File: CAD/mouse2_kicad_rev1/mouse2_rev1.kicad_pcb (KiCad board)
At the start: 2 copper layers, 101 parts, among them IC1 STM32F405RGT6, J2 SWD Header, M1 M1_Conn_Alt, M2 M2_Conn_Alt, Q0 TEFT4300, Q1 TEFT4300, Q10 Q_NMOS_GSD, Q11 Q_NMOS_GSD, Q12 Q_NMOS_GSD, Q2 TEFT4300, Q3 TEFT4300, Q9 Q_NMOS_GSD, SW1 SW, SW2 SW, SW3 SW, U10 TPS7A2033PDBVR, U2 L293D, U3 TLV70019_SOT23-5, U4 BC832, U5 LM66100DCKR, U6 LM66100DCKR, U7 ICM-45605, U8 TPS7A2033PDBVR, U9 TS30011-M050QFNR

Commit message: Mouse 2 is ballin ish! got a bunch of layout done
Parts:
- removed C38: 22uF, Capacitor_SMD:C_0805_2012Metric_Pad1.18x1.45mm_HandSolder
- removed C40: 0.1uF, Capacitor_SMD:C_0805_2012Metric_Pad1.18x1.45mm_HandSolder
- removed MOS1: SSM3K335R_LF, custom_foot:SOT-23F_TOS
- removed RST1, SW1, SW2, SW3: SW, Button_Switch_SMD:SW_SPST_REED_CT05-XXXX-G1
- removed U6: LM66100DCKR, custom_foot:DCK6_TEX
- added C10: 0.1uF, Capacitor_SMD:C_0603_1608Metric_Pad1.08x0.95mm_HandSolder, F.Cu at (210.6, 126.2)
- added C11: 0.1uF, Capacitor_SMD:C_0603_1608Metric_Pad1.08x0.95mm_HandSolder, F.Cu at (200.5, 111.1)
- added C12: 0.1uF, Capacitor_SMD:C_0603_1608Metric_Pad1.08x0.95mm_HandSolder, F.Cu at (188.0, 132.9)
- added C13: 4.7uF, Capacitor_SMD:C_0603_1608Metric_Pad1.08x0.95mm_HandSolder, F.Cu at (207.8, 110.6)
- added C16: 10uF, Capacitor_SMD:C_0603_1608Metric_Pad1.08x0.95mm_HandSolder, F.Cu at (202.5, 110.6)
- added C17: 0.1uF, Capacitor_SMD:C_0603_1608Metric_Pad1.08x0.95mm_HandSolder, F.Cu at (202.7, 108.3)
- added C18: 47uF, Capacitor_SMD:C_0603_1608Metric_Pad1.08x0.95mm_HandSolder, F.Cu at (233.2, 143.4)
- added C22: 15pF, Capacitor_SMD:C_0603_1608Metric_Pad1.08x0.95mm_HandSolder, F.Cu at (230.6, 141.6)
- added C23: 22uF, Capacitor_SMD:C_0603_1608Metric_Pad1.08x0.95mm_HandSolder, F.Cu at (165.0, 136.5)
- added C24: 15pF, Capacitor_SMD:C_0603_1608Metric_Pad1.08x0.95mm_HandSolder, F.Cu at (230.6, 139.0)
- added C25: 0.1uF, Capacitor_SMD:C_0603_1608Metric_Pad1.08x0.95mm_HandSolder, F.Cu at (166.0, 142.1)
- added C26: 10uF, Capacitor_SMD:C_0603_1608Metric_Pad1.08x0.95mm_HandSolder, F.Cu at (166.0, 144.1)
- added D10: LED, LED_SMD:LED_0805_2012Metric_Pad1.15x1.40mm_HandSolder, F.Cu at (120.7, 105.6)
- added D8: 1SS389,L3F, Diode_SMD:D_SOD-523, F.Cu at (120.1, 116.0)
- added D9: 1SS389,L3F, Diode_SMD:D_SOD-523, F.Cu at (120.1, 118.4)
- added J1: SWD Header, Connector_PinHeader_2.54mm:PinHeader_1x05_P2.54mm_Vertical, F.Cu at (125.4, 94.2)
- added R10: 10k, Resistor_SMD:R_0603_1608Metric_Pad0.98x0.95mm_HandSolder, F.Cu at (200.5, 126.8)
- added R22: 13, Resistor_SMD:R_0603_1608Metric_Pad0.98x0.95mm_HandSolder, F.Cu at (206.9, 126.2)
- added R23: 47K, Resistor_SMD:R_0603_1608Metric_Pad0.98x0.95mm_HandSolder, F.Cu at (117.6, 68.1)
- added R25: 47K, Resistor_SMD:R_0603_1608Metric_Pad0.98x0.95mm_HandSolder, F.Cu at (117.6, 73.1)
- added R28: 47K, Resistor_SMD:R_0603_1608Metric_Pad0.98x0.95mm_HandSolder, F.Cu at (117.6, 80.6)
- added S1: SKRPABE010, BUTTON:SW_SKRPABE010, F.Cu at (110.0, 94.3)
- added S3: SKRPABE010, BUTTON:SW_SKRPABE010, F.Cu at (110.0, 99.0)
- added S4: SKRPABE010, BUTTON:SW_SKRPABE010, F.Cu at (110.0, 103.8)
- added S6: SKRPABE010, BUTTON:SW_SKRPABE010, F.Cu at (110.0, 108.5)
- added U1: PMW3389DM-T3QU, PMW3389:PMW3360DM, F.Cu at (208.6, 113.5)
- added U11: LM66100DCKR, custom_foot:DCK6_TEX, F.Cu at (120.7, 112.8)
- added Y1: ABS07-32.768KHZ-T, AS07-XTAL:XTAL_ABS07-32.768KHZ-T, F.Cu at (233.7, 140.3)
- added Y2: 16MHz, Crystal:Crystal_SMD_2016-4Pin_2.0x1.6mm, F.Cu at (211.2, 135.5)
- C14, C15, C20, C27, C28, C29, C3, C30, C31, C32, C33, C34, C39, C8, C9: footprint Capacitor_SMD:C_1206_3216Metric_Pad1.33x1.80mm_HandSolder -> Capacitor_SMD:C_0603_1608Metric_Pad1.08x0.95mm_HandSolder
- C19: value 0.1uF -> 10uF; footprint Capacitor_SMD:C_1206_3216Metric_Pad1.33x1.80mm_HandSolder -> Capacitor_SMD:C_0603_1608Metric_Pad1.08x0.95mm_HandSolder
- C21: value 1uF -> 0.1uF; footprint Capacitor_SMD:C_1206_3216Metric_Pad1.33x1.80mm_HandSolder -> Capacitor_SMD:C_0603_1608Metric_Pad1.08x0.95mm_HandSolder
- C35, C36: value 10uF -> 0.1uF; footprint Capacitor_SMD:C_1206_3216Metric_Pad1.33x1.80mm_HandSolder -> Capacitor_SMD:C_0603_1608Metric_Pad1.08x0.95mm_HandSolder
- C37: footprint Capacitor_SMD:C_0805_2012Metric_Pad1.18x1.45mm_HandSolder -> Capacitor_SMD:C_0603_1608Metric_Pad1.08x0.95mm_HandSolder
- C4: value 0.1uF -> 1uF; footprint Capacitor_SMD:C_1206_3216Metric_Pad1.33x1.80mm_HandSolder -> Capacitor_SMD:C_0603_1608Metric_Pad1.08x0.95mm_HandSolder
- C7: value 10uF -> 0.1uF
- R1, R11, R19, R2, R20, R21, R24, R26, R3, R4, R5, R6, R7, R8, R9: footprint Resistor_SMD:R_1206_3216Metric_Pad1.30x1.75mm_HandSolder -> Resistor_SMD:R_0603_1608Metric_Pad0.98x0.95mm_HandSolder
- R12: value 47K -> 75; footprint Resistor_SMD:R_1206_3216Metric_Pad1.30x1.75mm_HandSolder -> Resistor_SMD:R_0603_1608Metric_Pad0.98x0.95mm_HandSolder
- R13, R14, R15: value 47k -> 47K; footprint Resistor_SMD:R_1206_3216Metric_Pad1.30x1.75mm_HandSolder -> Resistor_SMD:R_0603_1608Metric_Pad0.98x0.95mm_HandSolder
- R16: value 47k -> 10k; footprint Resistor_SMD:R_1206_3216Metric_Pad1.30x1.75mm_HandSolder -> Resistor_SMD:R_0603_1608Metric_Pad0.98x0.95mm_HandSolder
- R17, R27: value 10K -> 10k; footprint Resistor_SMD:R_1206_3216Metric_Pad1.30x1.75mm_HandSolder -> Resistor_SMD:R_0603_1608Metric_Pad0.98x0.95mm_HandSolder
- R18: value 20K -> 20k; footprint Resistor_SMD:R_1206_3216Metric_Pad1.30x1.75mm_HandSolder -> Resistor_SMD:R_0603_1608Metric_Pad0.98x0.95mm_HandSolder
- moved M1 186.9 mm to (288.8, 121.7), turned to 90 degrees
- moved M2 170.6 mm to (272.1, 121.7), turned to -90 degrees
- moved C3 160.2 mm to (295.0, 96.0)
- moved C35 152.2 mm to (303.7, 113.5)
- moved U2 148.1 mm to (276.6, 118.1)
- moved Q11 141.4 mm to (239.5, 79.9), turned to 180 degrees
- moved R3 127.7 mm to (244.8, 77.9), turned to 90 degrees
- moved R7 126.0 mm to (240.9, 76.9), turned to 180 degrees
- moved R15 120.8 mm to (242.8, 79.9), turned to 90 degrees
- moved U4 120.0 mm to (240.1, 142.3), turned to 180 degrees
- moved Q12 116.9 mm to (204.2, 71.9), turned to 180 degrees
- moved D2 114.3 mm to (241.5, 74.9), turned to 180 degrees
- moved C20 106.2 mm to (247.0, 77.9), turned to -90 degrees
- moved Q10 101.6 mm to (193.2, 73.8), turned to 180 degrees
- moved Q2 97.5 mm to (247.0, 74.9), turned to 180 degrees
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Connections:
- C1 pad 2: AGND -> GND
- C14 pad 1: +3V3A -> VDDA
- C14 pad 2: AGND -> GND
- C15 pad 1: +3V3A -> VDDA
- C15 pad 2: AGND -> GND
- C19 pad 1: RST -> VDDA
- C2 pad 1: +1V9 -> MOUSE_VDD
- C2 pad 2: AGND -> GND
- C20 pad 1: +3V3A -> VDDA
- C20 pad 2: AGND -> GND
- C21 pad 1: +3V3A -> GND
- C21 pad 2: AGND -> VDD
- C27 pad 1: VDD -> GND
- C27 pad 2: GND -> VDD
- C28 pad 1: VDD -> GND
- C28 pad 2: GND -> VDD
- C29 pad 1: VDD -> GND
- C29 pad 2: GND -> VDD
- C31 pad 1: VDDA -> GND
- C31 pad 2: GND -> VDDA
- C32 pad 1: VDD -> GND
- C32 pad 2: GND -> VDD
- C34 pad 1: VCAP_2 -> VCAP_1
- C35 pad 1: VDDA -> GND
- C35 pad 2: GND -> +5V
- C36 pad 1: BATT_NET -> Net-(D8-K)
- C36 pad 2: PGND -> GND
- C37 pad 1: +5V_NET -> +5V
- C4 pad 1: +5V -> VDDA
- C44 pad 1: +3V3A -> VDDA
- C44 pad 2: AGND -> GND
- C5 pad 1: unconnected-(C5-Pad1) -> MOUSE_VDD
- C5 pad 2: unconnected-(C5-Pad2) -> GND
- C6 pad 1: unconnected-(C6-Pad1) -> VDD
- C6 pad 2: unconnected-(C6-Pad2) -> GND
- C7 pad 1: unconnected-(C7-Pad1) -> VDD
- C7 pad 2: unconnected-(C7-Pad2) -> GND
- C8 pad 1: VDD -> GND
- C8 pad 2: GND -> VDD
- C9 pad 1: unconnected-(C9-Pad1) -> VDDPIX
- C9 pad 2: unconnected-(C9-Pad2) -> GND
- D7 pad 1: POWER_LED -> GND
- IC1 pad 12: VSSA -> GND
- IC1 pad 18: VSS -> GND
- IC1 pad 40: POWER_LED -> unconnected-(IC1-PC9-Pad40)
- IC1 pad 5: unconnected-(IC1-PH0-Pad5) -> Net-(IC1-PH0)
- IC1 pad 50: unconnected-(IC1-PA15-Pad50) -> MOUSE_CS
- IC1 pad 51: unconnected-(IC1-PC10-Pad51) -> BC_RX_STM_TX
- IC1 pad 52: unconnected-(IC1-PC11-Pad52) -> BC_TX_STM_RX
- IC1 pad 53: unconnected-(IC1-PC12-Pad53) -> MOUSE_PICO
- IC1 pad 55: unconnected-(IC1-PB3-Pad55) -> MOUSE_SCLK
- IC1 pad 56: unconnected-(IC1-PB4-Pad56) -> MOUSE_POCI
- IC1 pad 63: VSS -> GND
- L2 pad 2: +5V_NET -> +5V
- NT2 pad 2: AGND -> PGND
- Q0 pad 1: +3V3A -> VDDA
- Q1 pad 1: +3V3A -> VDDA
- Q2 pad 1: +3V3A -> VDDA
- Q3 pad 1: +3V3A -> VDDA
- R1 pad 1: AGND -> GND
- R12 pad 1: VDD -> Net-(D10-A)
- R12 pad 2: RST -> VDD
- R13 pad 1: GND -> EMIT_2
- R13 pad 2: EMIT_1 -> GND
- R14 pad 1: GND -> EMIT_3
- R14 pad 2: EMIT_2 -> GND
- R15 pad 1: GND -> EMIT_4
- R15 pad 2: EMIT_4 -> GND
- R16 pad 1: GND -> VDD
- R16 pad 2: EMIT_3 -> IMU_POCI
- R17 pad 1: GND -> BOOT0
- R17 pad 2: BOOT0 -> GND
- R2 pad 1: AGND -> GND
- R24 pad 1: VDD -> EMIT_1
- R24 pad 2: BUTTON_2 -> GND
- R3 pad 1: AGND -> GND
- R4 pad 1: AGND -> GND
- S2 pad 2: BATT_NET -> VCC
- U10 pad 2: AGND -> GND
- U10 pad 5: +3V3A -> VDDA
- U3 pad 2: AGND -> GND
- U3 pad 5: +1V9 -> MOUSE_VDD
- U4 pad 1: unconnected-(U4-GND-Pad1) -> GND
- U4 pad 10: unconnected-(U4-P21/RESET-Pad10) -> BC_RST
- U4 pad 11: unconnected-(U4-P00/XL1-Pad11) -> Net-(U4-P00/XL1)
- U4 pad 12: unconnected-(U4-P01/XL2-Pad12) -> Net-(U4-P01/XL2)
- U4 pad 16: unconnected-(U4-VDD-Pad16) -> VDD
- U4 pad 2: unconnected-(U4-P20/LED-Pad2) -> BC_LED
- U4 pad 3: unconnected-(U4-SWDIO-Pad3) -> BC_SWDIO
- U4 pad 4: unconnected-(U4-SWCLK-Pad4) -> BC_SWDCLK
- U4 pad 7: unconnected-(U4-P11/RX-Pad7) -> BC_RX_STM_TX
- U4 pad 8: unconnected-(U4-P12/TX-Pad8) -> BC_TX_STM_RX
- U5 pad 3: +5V_NET -> +5V
- U7 pad 5: +3V3A -> VDD
- U7 pad 6: AGND -> GND
- U7 pad 8: +3V3A -> VDDA
- U9 pad 11: BATT_NET -> VCC
- U9 pad 2: BATT_NET -> VCC
- U9 pad 3: BATT_NET -> VCC
- U9 pad 5: +5V_NET -> +5V
- U9 pad 9: BATT_NET -> unconnected-(U9-EN-Pad9)
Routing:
- net VDD: track 0.00 -> 63.8 mm
- net MOUSE_VDD: track 0.00 -> 50.3 mm
- net VCC: track 0.00 -> 36.8 mm, vias 0 -> 2
- net PGND: track 0.00 -> 29.3 mm, vias 0 -> 4
- net +5V: track 0.00 -> 22.6 mm
- net VDDA: track 0.00 -> 18.1 mm
- net Net-(C39-Pad2): track 0.00 -> 14.5 mm
- net IMU_CS: track 0.00 -> 14.2 mm, vias 0 -> 2
- net IMU_SCLK: track 0.00 -> 11.5 mm, vias 0 -> 2
- net IMU_PICO: track 0.00 -> 9.44 mm
- net IMU_POCI: track 0.00 -> 8.66 mm
- net Net-(U4-P00/XL1): track 0.00 -> 5.51 mm
- net GND: track 0.00 -> 4.92 mm, vias 0 -> 4
- net Net-(U4-P01/XL2): track 0.00 -> 4.89 mm
- net RECEIV_3: track 0.00 -> 4.80 mm
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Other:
- board outline added: 92.8 x 94.6 mm

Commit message: rev2 done !
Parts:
- removed C36: 0.1uF, Capacitor_SMD:C_0603_1608Metric_Pad1.08x0.95mm_HandSolder
- removed R10, R16: 10k, Resistor_SMD:R_0603_1608Metric_Pad0.98x0.95mm_HandSolder
- removed SK1, SK2, SK3, SK4: M2, MountingHole:MountingHole_2.2mm_M2
- removed TP7: V_EXT_TP, Connector_PinHeader_2.54mm:PinHeader_1x01_P2.54mm_Vertical
- added C38: 0.1uF, Capacitor_SMD:C_0603_1608Metric_Pad1.08x0.95mm_HandSolder, F.Cu at (232.0, 134.2)
- added C40: 0.1uF, Capacitor_SMD:C_0603_1608Metric_Pad1.08x0.95mm_HandSolder, F.Cu at (232.0, 130.2)
- moved R12 147.0 mm to (247.1, 133.8)
- moved R21 142.1 mm to (247.0, 121.8)
- moved R26 140.3 mm to (247.0, 129.8)
- moved C3 139.3 mm to (157.8, 119.4), turned to 90 degrees
- moved R9 139.1 mm to (237.3, 128.3), turned to 90 degrees
- moved R20 138.3 mm to (247.0, 125.8)
- moved R19 137.0 mm to (247.0, 117.8)
- moved S3 136.1 mm to (241.8, 128.3)
- moved RST1 134.3 mm to (241.8, 134.1)
- moved S2 133.9 mm to (241.8, 122.6)
- moved S1 132.4 mm to (241.8, 116.8)
- moved R11 132.4 mm to (237.3, 116.8), turned to 90 degrees
- moved R23 132.2 mm to (234.2, 130.2), turned to -90 degrees
- moved R25 131.7 mm to (234.2, 134.2), turned to -90 degrees
- moved D5 130.1 mm to (247.0, 127.8), turned to 180 degrees
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- renumbered M_MH2 to M_MH1, M_MH1 to M_MH2, S2 to PWR1, S6 to RST1, S4 to S1, S3 to S2, S1 to S3
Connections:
- M1 pad 1: M2_OUT_1 -> GND
- M1 pad 2: M2_OUT_2 -> M1_ENC_B
- M1 pad 3: VDD -> M1_ENC_A
- M1 pad 4: M2_ENC_A -> VDD
- M1 pad 5: M2_ENC_B -> M1_OUT_2
- M1 pad 6: GND -> M1_OUT_1
- M2 pad 1: M1_OUT_1 -> GND
- M2 pad 2: M1_OUT_2 -> M2_ENC_B
- M2 pad 3: VDD -> M2_ENC_A
- M2 pad 4: M1_ENC_A -> VDD
- M2 pad 5: M1_ENC_B -> M2_OUT_2
- M2 pad 6: GND -> M2_OUT_1
- PWR1 pad 3: Net-(S2-Pad3) -> unconnected-(PWR1-Pad3)
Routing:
- net +5V: track 22.6 -> 301.3 mm, vias 0 -> 1
- net VDD: track 63.8 -> 283.0 mm, vias 0 -> 11
- net VDDA: track 18.1 -> 198.9 mm
- net EMIT_4: track 2.33 -> 97.2 mm, vias 0 -> 2
- net RECEIV_4: track 2.21 -> 94.4 mm, vias 0 -> 1
- net EMIT_1: track 2.33 -> 82.7 mm, vias 0 -> 2
- net RECEIV_3: track 4.80 -> 85.1 mm, vias 0 -> 1
- net LED_RED: track 0.00 -> 79.6 mm, vias 0 -> 2
- net RECEIV_1: track 2.21 -> 79.5 mm, vias 0 -> 1
- net RECEIV_2: track 2.47 -> 79.0 mm, vias 0 -> 1
- net EMIT_3: track 2.33 -> 77.3 mm, vias 0 -> 2
- net LED_BLUE: track 0.00 -> 73.1 mm, vias 0 -> 2
- net EMIT_2: track 2.33 -> 71.5 mm, vias 0 -> 2
- net M1_ENC_A: track 0.00 -> 68.1 mm, vias 0 -> 2
- net M1_ENC_B: track 0.00 -> 67.0 mm, vias 0 -> 2
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- added copper zone on B.Cu, net GND
- added copper zone on F.Cu, net GND
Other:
- board text added: "AirLiteTalonFX"
- board text added: "Rev. 2.0 | By Rezq"

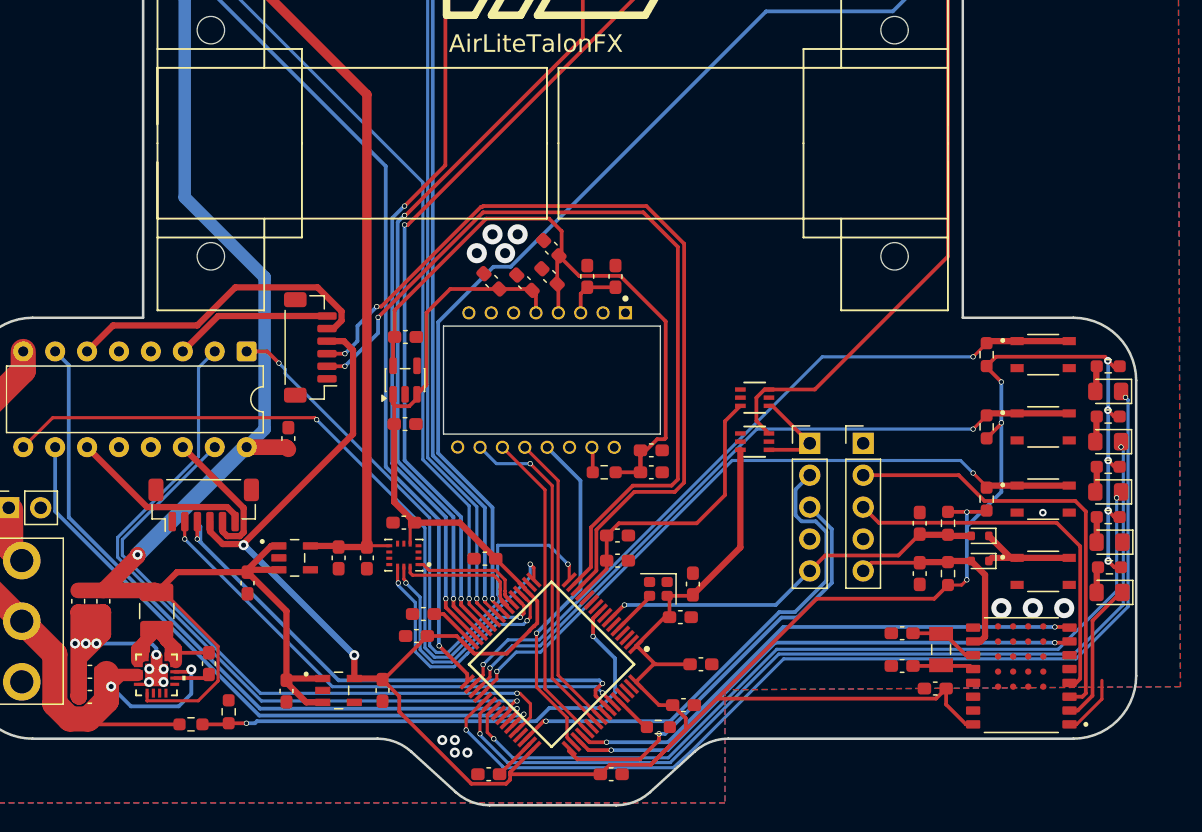
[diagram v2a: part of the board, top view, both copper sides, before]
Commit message: Micromouse is assembled and turns on! LEDs work as well. IOC is updated.
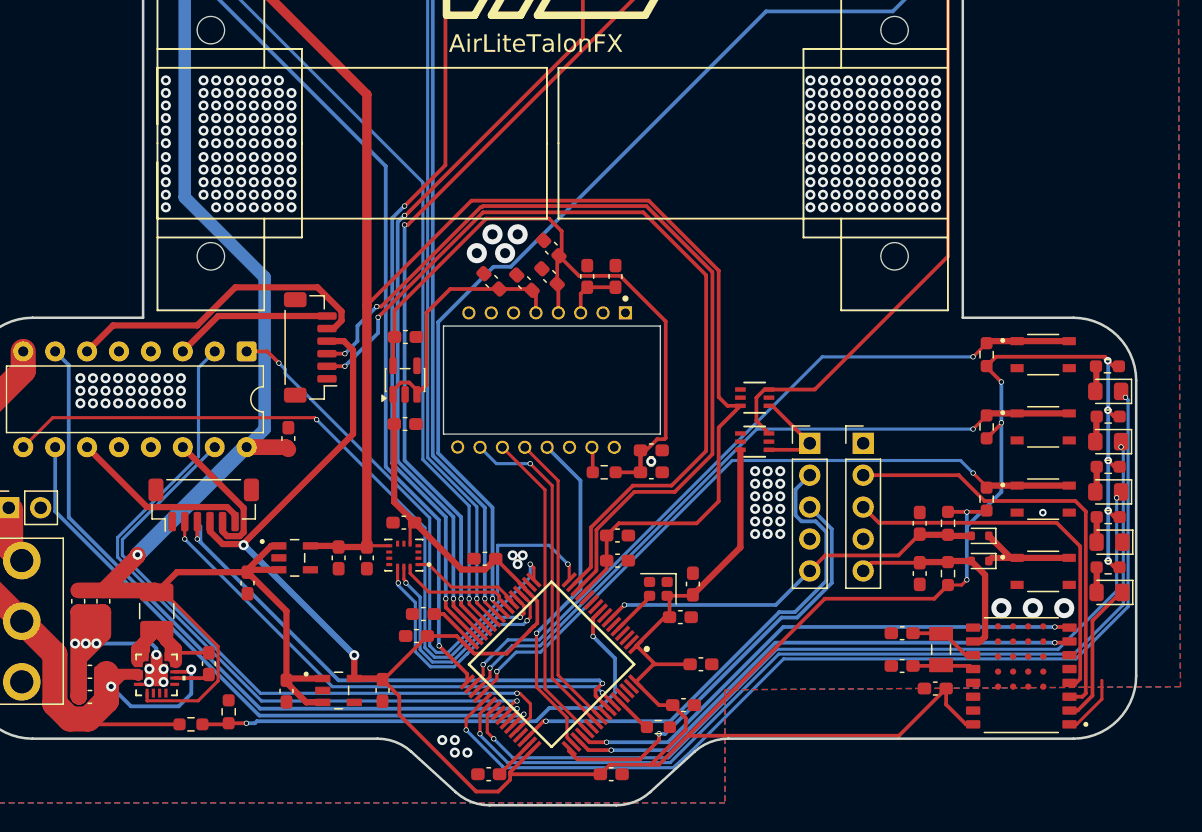
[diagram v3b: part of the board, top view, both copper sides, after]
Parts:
- moved R12 0.11 mm to (247.0, 133.8)
- moved R19 0.06 mm to (246.9, 117.8)
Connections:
- U7 pad 4: IMU_INT -> unconnected-(U7-INT1/INT-Pad4)
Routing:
- net VDDA: track 198.9 -> 244.7 mm
- net VDD: track 283.0 -> 288.5 mm
- net M1_ENC_B: track 67.0 -> 68.8 mm
- net M1_ENC_A: track 68.1 -> 70.0 mm
- net IMU_PICO: track 10.2 -> 9.49 mm
- net IMU_POCI: track 9.40 -> 8.74 mm
- net GND: vias 16 -> 283
